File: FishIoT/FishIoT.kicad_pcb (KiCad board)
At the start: 4 copper layers, 72.4 x 56.1 mm, 123 parts, among them IC1 RV-3032-C7_32.768KHZ-2.5PPM-T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, J1 VDD_JUMPER, J10 RM_UART, J2 0705430001, J3 SF72S006VBDR2500, J4 SHF-105-01-L-D-SM, J5 10119313-302TLF, J6 Conn_01x02_Socket, J7 Conn_01x02_Socket, J8 BM05B-ZESS-TBT, J9 SHF-105-01-L-D-SM, SW1 PTS645SM43SMTR92 LF, SW2 PTS645SM43SMTR92 LF, SW3 PTS645SM43SMTR92 LF, U1 NRF9160-SICA, U10 RM126x, U2 SKY65943-11, U3 TPD3F303DPVR, U4 TPS63000, U5 USBLC6-2P6, U6 CP2102N-Axx-xQFN20, U7 NX3020NAKV, U8 NX3020NAKV, U9 MAX3471

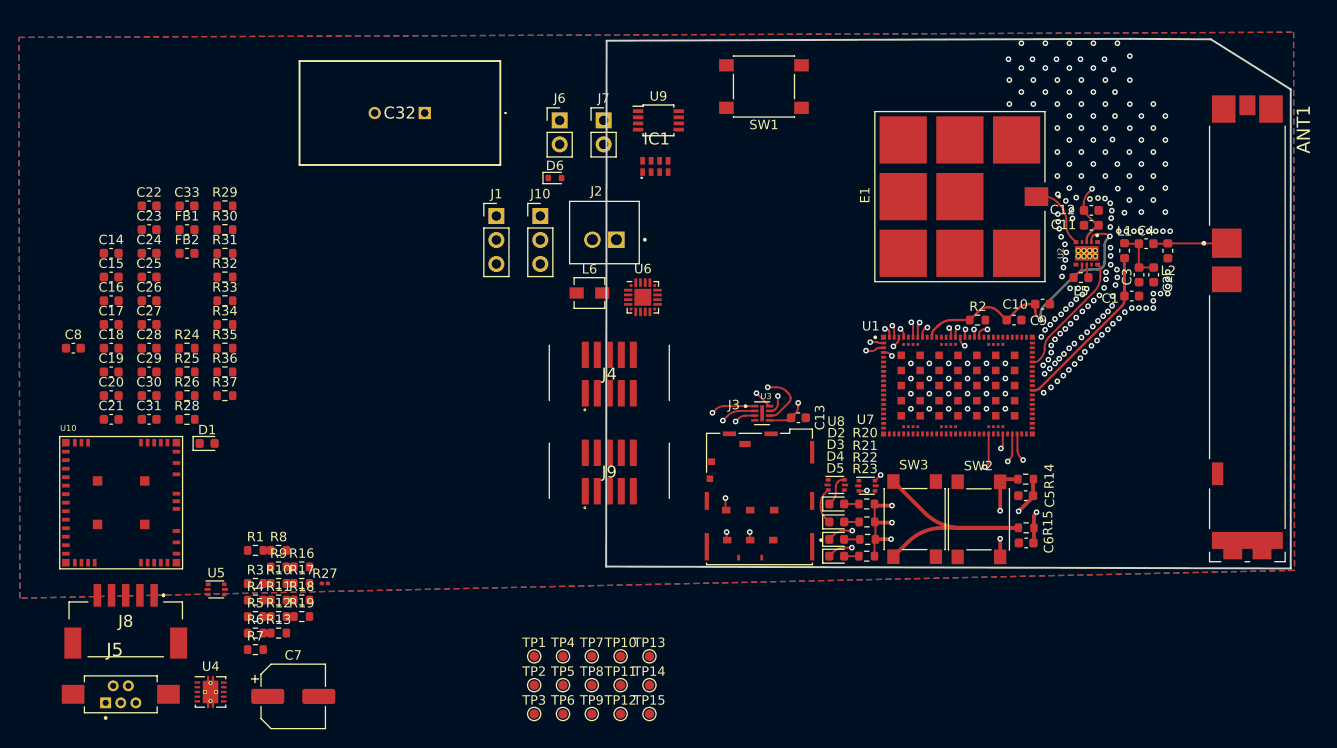
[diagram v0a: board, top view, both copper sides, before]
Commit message: Changed GNSS antenna into u.fl. connector, decreased size of pcb further
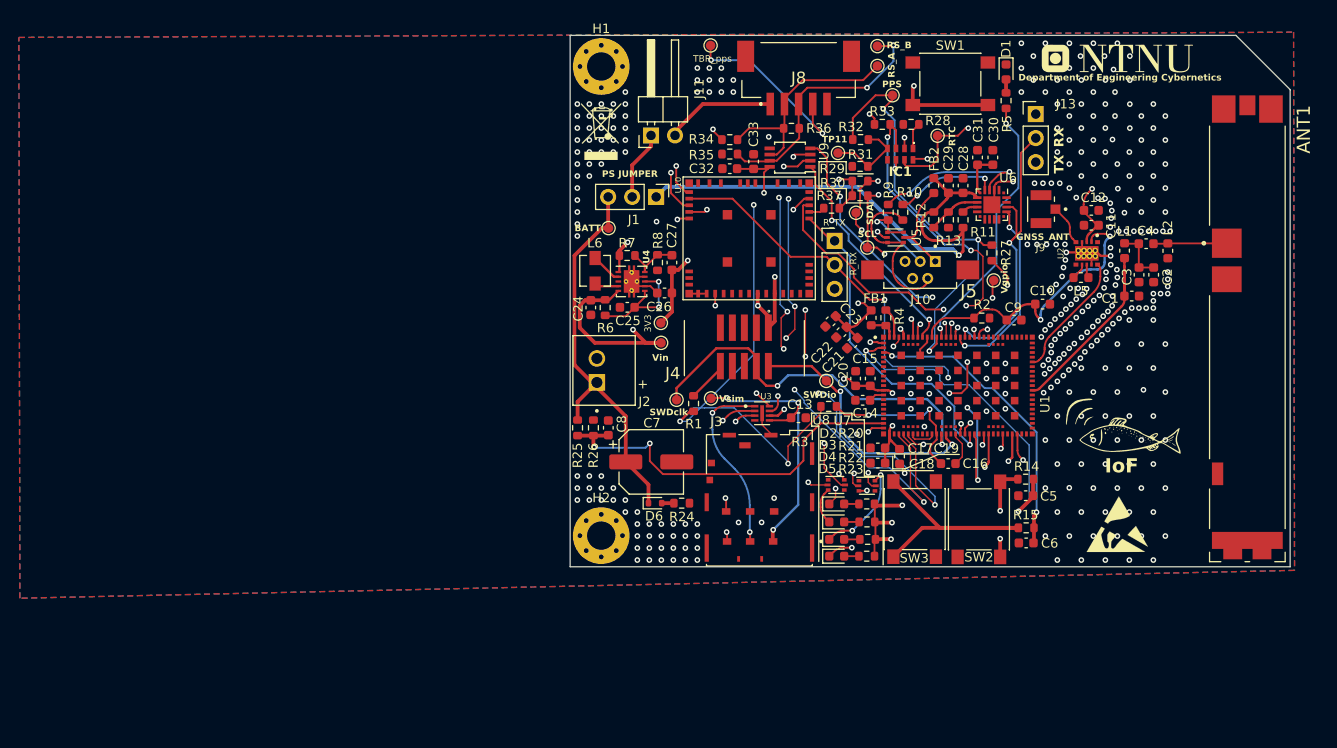
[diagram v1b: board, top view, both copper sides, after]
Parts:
- removed E1: DSGP.1575.18.4.A.02, FishIoT_Footprint_library:XCVR_DSGP.1575.18.4.A.02
- removed J6, J7: Conn_01x02_Socket, Connector_PinHeader_2.54mm:PinHeader_1x02_P2.54mm_Vertical
- removed R16, R17, R18, R19: 1M, Resistor_SMD:R_0603_1608Metric
- added G***: LOGO, FishIoT_Footprint_library:NTNUlogo2, F.Cu at (222.2, 58.7)
- added G***: LOGO, FishIoT_Footprint_library:Fishlogo, F.Cu at (223.1, 98.2)
- added H1: MountingHole_Pad, MountingHole:MountingHole_3mm_Pad_Via, F.Cu at (167.6, 59.5)
- added H2: MountingHole_Pad, MountingHole:MountingHole_3mm_Pad_Via, F.Cu at (167.6, 109.2)
- added J11: Current Measurement, Connector_PinHeader_2.54mm:PinHeader_1x02_P2.54mm_Horizontal, F.Cu at (172.9, 66.8)
- added J13: UART_DEBUG, Connector_PinHeader_2.54mm:PinHeader_1x03_P2.54mm_Vertical, F.Cu at (213.6, 64.6)
- added REF**: WEEE-Logo_4.2x6mm_SilkScreen, Symbol:WEEE-Logo_4.2x6mm_SilkScreen, F.Cu at (167.6, 66.4)
- added REF**: ESD-Logo_6.6x6mm_SilkScreen, Symbol:ESD-Logo_6.6x6mm_SilkScreen, F.Cu at (222.2, 108.0)
- C32: value PHVL-3R9V255-R -> 0.1u; footprint FishIoT_Footprint_library:PHVL3R9V255R -> Capacitor_SMD:C_0603_1608Metric
- J9: value SHF-105-01-L-D-SM -> Conn_Coaxial; footprint FishIoT_Footprint_library:SHF-105-01-X-D-SM -> FishIoT_Footprint_library:LINX_CONUFL001-SMD-T
- R27: footprint Resistor_SMD:R_0201_0603Metric -> Resistor_SMD:R_0603_1608Metric
- R34, R35: value 680 -> 10k
- moved R5 96.4 mm to (210.5, 63.1), turned to 90 degrees
- moved J5 95.8 mm to (201.4, 81.1), turned to 180 degrees
- moved D1 93.2 mm to (210.5, 60.1), turned to -90 degrees
- moved C30 92.8 mm to (209.1, 69.2), turned to -90 degrees
- moved J8 92.1 mm to (188.5, 60.3), turned to 180 degrees
- moved C31 91.9 mm to (207.5, 69.2), turned to -90 degrees
- moved C16 90.2 mm to (204.3, 101.5), turned to 180 degrees
- moved C28 87.8 mm to (205.9, 72.1), turned to -90 degrees
- moved C29 86.9 mm to (204.4, 72.1), turned to -90 degrees
- moved C19 83.9 mm to (199.2, 100.8), turned to -90 degrees
- moved R13 83.3 mm to (204.4, 75.8), turned to 90 degrees
- moved R11 82.9 mm to (205.9, 75.8), turned to 90 degrees
- moved R28 82.7 mm to (200.4, 65.7)
- moved C17 82.2 mm to (196.9, 99.9), turned to 180 degrees
- moved C18 82.0 mm to (196.9, 101.5), turned to 180 degrees
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- renumbered TP7 to 3V3, TP8 to BATT, TP6 to PPS, TP13 to RS_A, TP14 to RS_B, TP12 to RTC, TP10 to SCL, TP9 to SDA, TP3 to SWDclk, TP2 to SWDio, TP15 to TBR_pps, TP5 to Vgpio, TP1 to Vin, TP4 to Vsim
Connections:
- C32 pad 1: +BATT -> GND
- C32 pad 2: GND -> +3V3
- J1 pad 2: /VREG_IN -> /VIN
- J9 pad 1: +3V3 -> /GPS_RF_ANT
- J9 pad 3: /RM_RESETn -> (no net)
- R34 pad 2: Net-(J7-Pin_2) -> +3V3
- R35 pad 1: Net-(J6-Pin_1) -> GND
- U10 pad 37: /RM_SWCLK -> unconnected-(U10-PA01-Pad37)
- U10 pad 38: /RM_SWDIO -> unconnected-(U10-PA02-Pad38)
- U10 pad 39: /RM_SWO -> unconnected-(U10-PA03-Pad39)
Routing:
- net /~{nRESET}: track 0.00 -> 83.7 mm, vias 0 -> 4
- net /TBR_PPS: track 0.00 -> 66.5 mm, vias 0 -> 5
- net +3V3: track 18.2 -> 80.6 mm, vias 4 -> 20
- net /VREG_IN: track 0.00 -> 60.0 mm, vias 0 -> 1
- net /RS485_DE: track 0.00 -> 58.2 mm, vias 0 -> 6
- net /RM_RX: track 0.00 -> 56.5 mm, vias 0 -> 4
- net /RS485_RE: track 0.00 -> 55.4 mm, vias 0 -> 6
- net VBUS: track 0.00 -> 55.0 mm, vias 0 -> 1
- net /RM_CTS: track 0.00 -> 53.8 mm, vias 0 -> 2
- net /nINT_RTC: track 0.00 -> 53.6 mm, vias 0 -> 6
- net /RM_RTS: track 0.00 -> 52.5 mm, vias 0 -> 2
- net /PPS: track 0.00 -> 47.1 mm, vias 0 -> 3
- net +BATT: track 0.00 -> 42.7 mm
- net /Battery_voltage: track 0.00 -> 41.5 mm, vias 0 -> 2
- net GND: track 0.36 -> 41.0 mm, vias 201 -> 338
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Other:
- board size 72.4 x 56.1 mm -> 76.2 x 56.2 mm
- board text added: "+"
- board text added: "Department of Engineering Cybernetics"
- board text added: "GNSS_ANT"
- board text added: "IoF"
- board text added: "PS JUMPER"
- board text added: "RX"
- board text added: "R_RX"
- board text added: "R_TX"
- board text added: "TX"

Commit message: updated schematic and pcb
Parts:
- removed C3: N.C., Capacitor_SMD:C_0603_1608Metric
- removed C4: 3.5pF, Capacitor_SMD:C_0603_1608Metric
- removed R28: 10k, Resistor_SMD:R_0603_1608Metric
- added BT1: 3002, FishIoT_Footprint_library:BAT_3002, B.Cu at (197.3, 67.0)
- added G***: LOGO, FishIoT_Footprint_library:ntnulogoLARGE, B.Cu at (202.4, 98.8)
- added H3: MountingHole_Pad, MountingHole:MountingHole_3mm_Pad_Via, F.Cu at (223.5, 65.3)
- added L3: L, Inductor_SMD:L_0603_1608Metric, F.Cu at (216.4, 79.9)
- added L4: 33nH, Inductor_SMD:L_0603_1608Metric, F.Cu at (220.2, 79.0)
- added R16: R, Resistor_SMD:R_0603_1608Metric, F.Cu at (218.7, 79.0)
- added R17: 120, Resistor_SMD:R_0603_1608Metric, F.Cu at (207.8, 65.5)
- C1: value N.C. -> C
- C2: value N.C. -> 100n
- C33: value 100n -> 0.1u
- R5: value 180 -> 120
- RTC_EVI1: renamed from TP11; value TestPoint -> RTC_EVI
- moved C2 27.8 mm to (203.4, 65.5), turned to 0 degrees
- moved R2 10.7 mm to (218.5, 85.3), turned to 90 degrees
- moved C1 9.22 mm to (216.4, 78.3), turned to 180 degrees
- moved C9 8.81 mm to (220.1, 85.3), turned to -90 degrees
- moved C12 7.57 mm to (218.5, 82.3), turned to 90 degrees
- moved C10 7.28 mm to (221.6, 85.3), turned to 90 degrees
- moved C11 5.96 mm to (220.1, 82.3), turned to -90 degrees
- moved L5 5.75 mm to (213.4, 84.6), turned to 90 degrees
- moved U2 5.13 mm to (216.0, 83.5), turned to 180 degrees
- moved RTC_CO1 4.82 mm to (208.0, 67.3)
- moved J9 4.62 mm to (218.8, 74.9), turned to -90 degrees
- moved Vin1 3.27 mm to (176.8, 90.4)
- moved PPS1 3.26 mm to (201.4, 61.2)
- moved REF** 3.00 mm to (170.6, 66.5)
- moved J10 3.00 mm to (195.3, 78.1)
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- renumbered PPS to PPS1, RS_A to RS_A1, RS_B to RS_B1, RTC to RTC_CO1, SCL to SCL1, SDA to SDA1, SWDclk to SWDCLK1, SWDio to SWDIO1, TBR_pps to TBR_PPS1, Vsim to VSIM1, BATT to Vbat1, Vgpio to Vgpio1, Vin to Vin1, 3V3 to Vout1
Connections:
- C1 pad 1: /LTE_RF1 -> Net-(J9-In)
- C2 pad 1: Net-(C2-Pad1) -> GND
- C2 pad 2: GND -> Net-(IC1-VBACKUP)
- H1 pad 1: unconnected-(H1-Pad1) -> GND
- H2 pad 1: unconnected-(H2-Pad1) -> GND
- J9 pad 1: /GPS_RF_ANT -> Net-(J9-In)
- L1 pad 2: Net-(C2-Pad1) -> Net-(ANT1-FEED)
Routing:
- net Net-(J9-In): track 0.00 -> 6.51 mm
- net Net-(C2-Pad1): track 5.60 -> 0.00 mm
- net /GPS_RF1: track 13.4 -> 7.90 mm
- net /VREG_IN: track 60.0 -> 64.9 mm
- net /GPS_EN: track 31.0 -> 26.5 mm
- net Net-(BT1-PadP1): track 0.00 -> 3.08 mm, vias 0 -> 1
- net +3V3: track 80.6 -> 83.5 mm, vias 20 -> 21
- net Net-(IC1-VBACKUP): track 2.81 -> 5.53 mm
- net GND: track 41.0 -> 38.9 mm, vias 338 -> 224
- net Net-(U2-AMP_IN): track 1.43 -> 2.75 mm
- net /RTC_CLOCKOUT: track 36.7 -> 35.6 mm
- net /PPS: track 47.1 -> 48.0 mm
- net /nRF_UART_RX: track 32.8 -> 31.9 mm
- net /nRF_UART_TX: track 27.9 -> 27.0 mm
- net /LTE_RF1: track 18.3 -> 17.5 mm
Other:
- board size 76.2 x 56.2 mm -> 71.4 x 56.4 mm

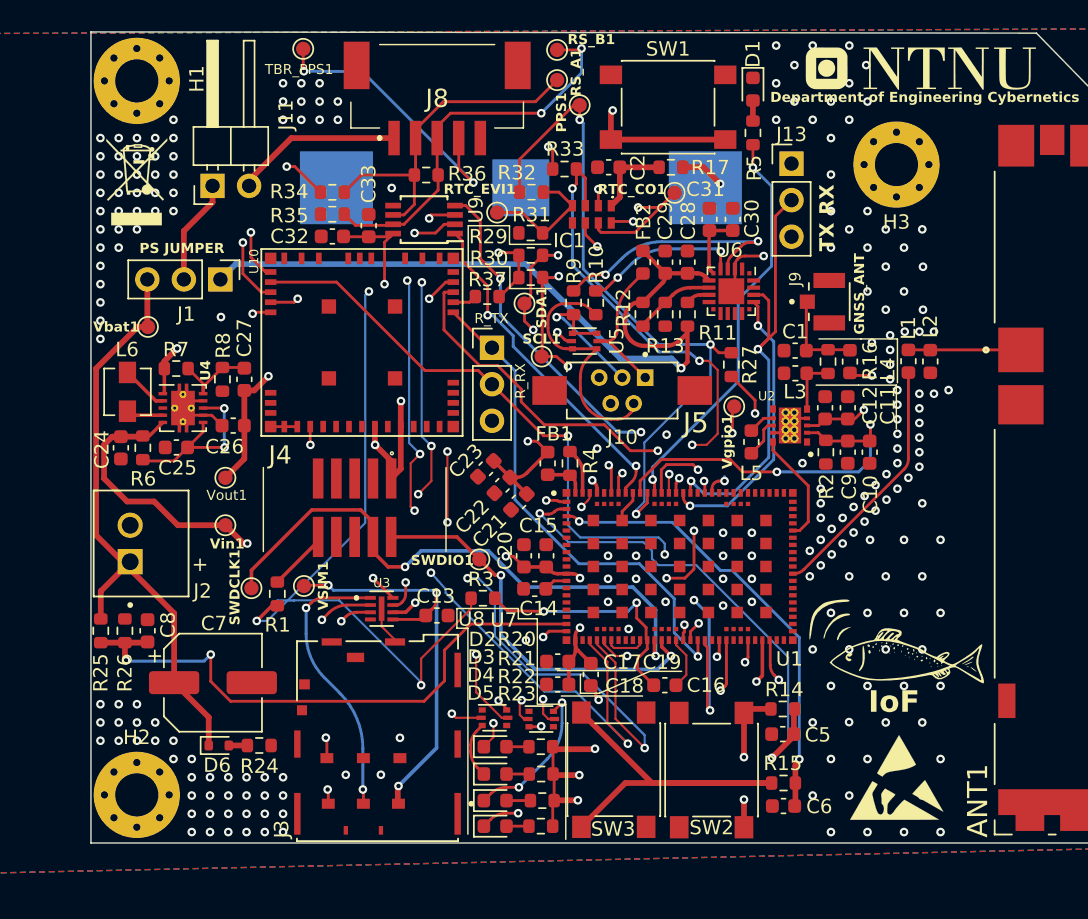
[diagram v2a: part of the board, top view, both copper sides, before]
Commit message: removed MOS for leds, added RS connector
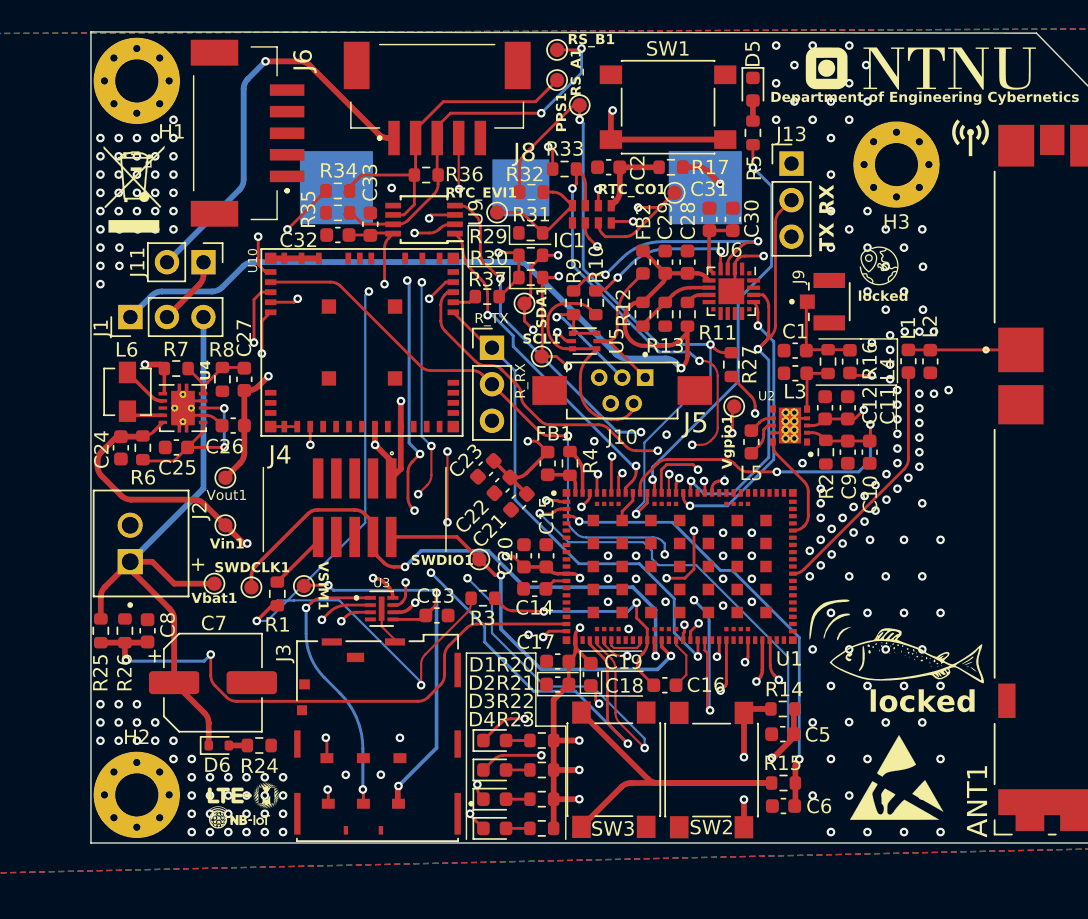
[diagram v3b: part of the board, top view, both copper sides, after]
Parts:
- removed TBR_PPS1: TestPoint, TestPoint:TestPoint_Pad_D1.0mm
- removed U7, U8: NX3020NAKV, Package_TO_SOT_SMD:SOT-666
- added G***: LOGO, FishIoT_Footprint_library:nbiotlogo, F.Cu at (177.8, 110.7)
- added G***: LOGO, FishIoT_Footprint_library:batterylogoo, B.Cu at (176.0, 80.0)
- added G***: LOGO, FishIoT_Footprint_library:antennalogo, F.Cu at (228.6, 63.5)
- added G***: LOGO, FishIoT_Footprint_library:lte-mlogo, F.Cu at (178.1, 109.2)
- added G***: LOGO, FishIoT_Footprint_library:gnsslogo, F.Cu at (222.2, 72.4)
- added G***: LOGO, FishIoT_Footprint_library:ammeterlogo, B.Cu at (174.0, 69.6)
- added G***: LOGO, FishIoT_Footprint_library:usblogo, B.Cu at (169.9, 80.0)
- added J6: BM05B-ZESS-TBT, FishIoT_Footprint_library:BM05BZESSTBTLFSN, F.Cu at (177.9, 63.2)
- J11: footprint Connector_PinHeader_2.54mm:PinHeader_1x02_P2.54mm_Horizontal -> Connector_PinHeader_2.54mm:PinHeader_1x02_P2.54mm_Vertical
- moved Vbat1 18.4 mm to (176.0, 94.5)
- moved J1 6.78 mm to (170.2, 75.9), turned to 90 degrees
- moved J11 5.35 mm to (175.3, 72.1), turned to -90 degrees
- moved D1 4.18 mm to (195.5, 105.4)
- moved R20 4.18 mm to (198.8, 105.4)
- moved R21 3.91 mm to (198.8, 107.4)
- moved D2 3.91 mm to (195.5, 107.4)
- moved R23 3.78 mm to (198.8, 111.5)
- moved D4 3.78 mm to (195.5, 111.5)
- moved R22 3.65 mm to (198.8, 109.5)
- moved D3 3.65 mm to (195.5, 109.5)
- moved REF** 0.54 mm to (170.4, 67.1)
- moved C32 0.39 mm to (184.6, 70.2)
- moved R34 0.39 mm to (184.6, 67.2)
- moved R35 0.39 mm to (184.6, 68.7)
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- renumbered D4 to D1, D5 to D2, D2 to D3, D3 to D4, D1 to D5, R22 to R20, R23 to R21, R20 to R22, R21 to R23
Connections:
- D1 pad 1: Net-(D4-K) -> /nRF91_LED1
- D2 pad 1: Net-(D5-K) -> /nRF91_LED2
- D3 pad 1: Net-(D2-K) -> /nRF91_LED3
- D4 pad 1: Net-(D3-K) -> /nRF91_LED4
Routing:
- net /TBR_PPS: track 66.5 -> 47.5 mm, vias 5 -> 4
- net Net-(D4-K): track 10.6 -> 0.00 mm, vias 2 -> 0
- net Net-(D5-K): track 10.4 -> 0.00 mm, vias 2 -> 0
- net /VREG_IN: track 64.9 -> 72.6 mm, vias 1 -> 2
- net VBUS: track 55.0 -> 62.1 mm
- net /nRF91_LED2: track 20.1 -> 26.8 mm
- net /nRF91_LED4: track 20.3 -> 27.0 mm
- net /RM_RTS: track 52.5 -> 46.2 mm
- net +3V3: track 83.5 -> 89.1 mm
- net Net-(D2-K): track 4.53 -> 0.00 mm, vias 2 -> 0
- net /nRF91_LED1: track 23.1 -> 27.1 mm
- net Net-(D3-K): track 3.94 -> 0.00 mm
- net GND: track 38.9 -> 42.4 mm, vias 224 -> 212
- net +BATT: track 42.7 -> 45.3 mm
- net /VIN: track 7.33 -> 4.82 mm
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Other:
- board text added: "-"
- board text added: "locked"
- board text removed: "GNSS_ANT"
- board text removed: "IoF"
- board text removed: "PS JUMPER"
